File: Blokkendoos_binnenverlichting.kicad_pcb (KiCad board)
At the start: 2 copper layers, 206.8 x 26 mm, 103 parts, among them J1 Conn_01x02, J10 Conn_01x04, J11 Conn_01x04, J12 Conn_01x04, J13 Conn_01x04, J14 Conn_01x04, J15 Conn_01x04, J16 Conn_01x02, J2 Conn_02x11_Counter_Clockwise, J3 Conn_01x04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

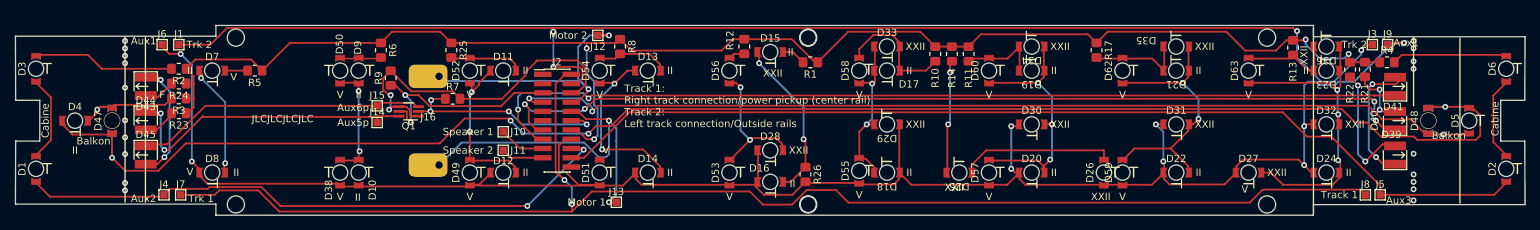
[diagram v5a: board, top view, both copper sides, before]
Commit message: Pulled traces away from edge, making room to cut the corners and/or PCB to shape. Closes #11.
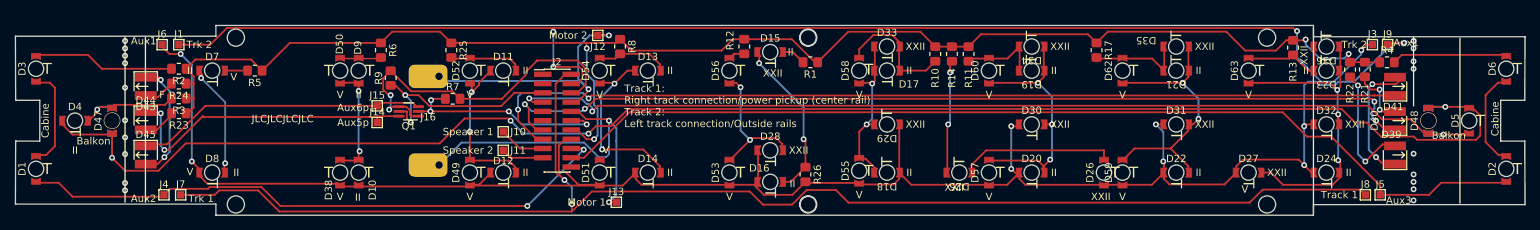
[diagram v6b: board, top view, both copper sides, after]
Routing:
- net Net-(D1-Pad2): track 11.6 -> 14.0 mm
- net Net-(D2-Pad2): track 11.4 -> 13.6 mm
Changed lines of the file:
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@@
   (segment (start 126.882304 132.08) (end 133.113771 125.848533) (width 0.25) (layer "F.Cu") (net 13))
   (segment (start 125.14 132.08) (end 126.882304 132.08) (width 0.25) (layer "F.Cu") (net 13))
-  (segment (start 251.582 137.16) (end 235.966 137.16) (width 0.25) (layer "F.Cu") (net 13))
   (segment (start 225.949786 129.1844) (end 229.2604 129.1844) (width 0.25) (layer "F.Cu") (net 13))
   (segment (start 133.113771 125.848533) (end 222.613919 125.848533) (width 0.25) (layer "F.Cu") (net 13))
+  (segment (start 253.238 135.504) (end 244.317 135.504) (width 0.25) (layer "F.Cu") (net 13))
+  (segment (start 242.661 137.16) (end 235.966 137.16) (width 0.25) (layer "F.Cu") (net 13))
+  (segment (start 244.317 135.504) (end 242.661 137.16) (width 0.25) (layer "F.Cu") (net 13))
   (segment (start 235.966 135.89) (end 235.966 137.16) (width 0.25) (layer "F.Cu") (net 13))
-  (segment (start 253.238 135.504) (end 251.582 137.16) (width 0.25) (layer "F.Cu") (net 13))
-  (segment (start 53.726 137.414) (end 69.088 137.414) (width 0.25) (layer "F.Cu") (net 14))
+  (segment (start 54.904 135.504) (end 56.814 137.414) (width 0.25) (layer "F.Cu") (net 14))
+  (segment (start 56.814 137.414) (end 69.088 137.414) (width 0.25) (layer "F.Cu") (net 14))
+  (segment (start 75.591674 136.0932) (end 82.7024 136.0932) (width 0.25) (layer "F.Cu") (net 14))
+  (segment (start 51.816 135.504) (end 54.904 135.504) (width 0.25) (layer "F.Cu") (net 14))
+  (segment (start 125.14 130.81) (end 126.685402 130.81) (width 0.25) (layer "F.Cu") (net 14))
   (segment (start 69.088 137.414) (end 69.342 137.16) (width 0.25) (layer "F.Cu") (net 14))
-  (segment (start 75.591674 136.0932) (end 82.7024 136.0932) (width 0.25) (layer "F.Cu") (net 14))
-  (segment (start 125.14 130.81) (end 126.685402 130.81) (width 0.25) (layer "F.Cu") (net 14))
   (segment (start 70.166511 136.335489) (end 75.349385 136.335489) (width 0.25) (layer "F.Cu") (net 14))
   (segment (start 85.2932 138.684) (end 119.126 138.684) (width 0.25) (layer "F.Cu") (net 14))
   (segment (start 126.685402 130.81) (end 126.842701 130.967299) (width 0.25) (layer "F.Cu") (net 14))
   (segment (start 82.7024 136.0932) (end 85.2932 138.684) (width 0.25) (layer "F.Cu") (net 14))
-  (segment (start 51.816 135.504) (end 53.726 137.414) (width 0.25) (layer "F.Cu") (net 14))
   (segment (start 69.342 137.16) (end 70.166511 136.335489) (width 0.25) (layer "F.Cu") (net 14))
   (segment (start 75.349385 136.335489) (end 75.591674 136.0932) (width 0.25) (layer "F.Cu") (net 14))
@@
   (segment (start 68.9 126) (end 68.9 130.5) (width 0.25) (layer "B.Cu") (net 54))
   (segment (start 68.9 130.5) (end 69.4 131) (width 0.25) (layer "B.Cu") (net 54))
-  (segment (start 51.816 131.704) (end 53.848 129.672) (width 0.25) (layer "F.Cu") (net 55))
-  (segment (start 53.848 123.82) (end 51.816 121.788) (width 0.25) (layer "F.Cu") (net 55))
-  (segment (start 53.848 129.672) (end 53.848 123.82) (width 0.25) (layer "F.Cu") (net 55))
-  (segment (start 253.238 131.704) (end 251.46 129.926) (width 0.25) (layer "F.Cu") (net 56))
-  (segment (start 251.46 123.566) (end 253.238 121.788) (width 0.25) (layer "F.Cu") (net 56))
-  (segment (start 251.46 129.926) (end 251.46 123.566) (width 0.25) (layer "F.Cu") (net 56))
+  (segment (start 54.4 130.5) (end 54.4 122.5) (width 0.25) (layer "F.Cu") (net 55))
+  (segment (start 54.4 122.5) (end 53.688 121.788) (width 0.25) (layer "F.Cu") (net 55))
+  (segment (start 51.816 131.704) (end 53.196 131.704) (width 0.25) (layer "F.Cu") (net 55))
+  (segment (start 53.196 131.704) (end 54.4 130.5) (width 0.25) (layer "F.Cu") (net 55))
+  (segment (start 53.688 121.788) (end 51.816 121.788) (width 0.25) (layer "F.Cu") (net 55))
+  (segment (start 252.112 121.788) (end 253.238 121.788) (width 0.25) (layer "F.Cu") (net 56))
+  (segment (start 250.4 129.933) (end 250.4 123.5) (width 0.25) (layer "F.Cu") (net 56))
+  (segment (start 250.4 123.5) (end 252.112 121.788) (width 0.25) (layer "F.Cu") (net 56))
+  (segment (start 252.171 131.704) (end 250.4 129.933) (width 0.25) (layer "F.Cu") (net 56))
+  (segment (start 253.238 131.704) (end 252.171 131.704) (width 0.25) (layer "F.Cu") (net 56))
   (segment (start 68.362 128.25) (end 66.04 128.25) (width 0.25) (layer "F.Cu") (net 57))
   (segment (start 70.39 126.222) (end 68.362 128.25) (width 0.25) (layer "F.Cu") (net 57))

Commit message: Added connectors for powerpack and DRC passes, except for silkscreen
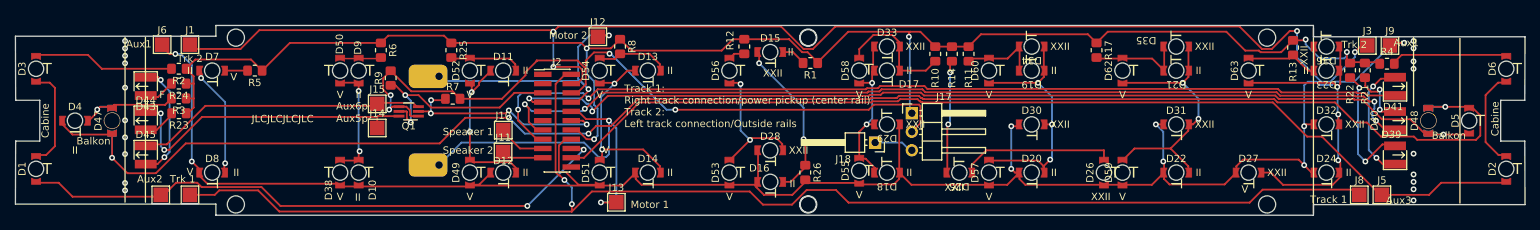
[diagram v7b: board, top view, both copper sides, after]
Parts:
- added J17: Conn_01x03_Female, Connector_PinHeader_2.54mm:PinHeader_1x03_P2.54mm_Horizontal, F.Cu at (171.8, 126.0)
- added J18: Conn_01x01, Connector_PinHeader_2.54mm:PinHeader_1x01_P2.54mm_Horizontal, F.Cu at (166.8, 130.0)
- J1, J10, J11, J12, J13, J14, J15, J3, J4, J5, J6, J7, J8, J9: footprint TestPoint:TestPoint_Pad_1.0x1.0mm -> TestPoint:TestPoint_Pad_2.0x2.0mm
- moved J1 1.53 mm to (72.9, 116.6)
- moved J7 1.27 mm to (72.9, 137.2)
- moved J8 0.83 mm to (233.1, 137.2)
- moved J14 0.75 mm to (98.6, 128.0)
- moved J3 0.71 mm to (234.2, 116.7)
- moved J4 0.44 mm to (68.9, 137.2)
- moved J9 0.34 mm to (237.3, 116.7)
- moved J15 0.27 mm to (98.6, 124.7)
- moved R26 0.27 mm to (157.2, 134.1)
- moved J11 0.24 mm to (115.8, 131.3)
- moved J5 0.23 mm to (236.2, 137.2)
- moved J10 0.22 mm to (115.8, 128.3)
- moved R4 0.20 mm to (236.9, 119.2)
- moved J12 0.18 mm to (128.8, 115.5)
- moved R21 0.12 mm to (233.9, 120.1)
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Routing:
- net GND: track 47.4 -> 102.5 mm, vias 2 -> 4
- net VPP: track 206.4 -> 217.4 mm, vias 4 -> 5
- net /Charge: track 0.00 -> 5.19 mm
- net /Gleis 1: track 189.4 -> 187.1 mm
- net /Motor2: track 48.9 -> 51.1 mm
- net /Gleis 2: track 184.7 -> 186.9 mm
- net Net-(D4-Pad1): track 222.4 -> 224.3 mm
- net /Aux4: track 135.9 -> 137.4 mm
- net Net-(D13-Pad1): track 25.3 -> 26.7 mm
- net /F0r: track 130.7 -> 131.8 mm
- net /F0f: track 128.5 -> 129.6 mm
- net /Aux3: track 136.8 -> 137.5 mm
- net /Aux5: track 29.7 -> 30.3 mm

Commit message: Silkscreen fixes, closes #10
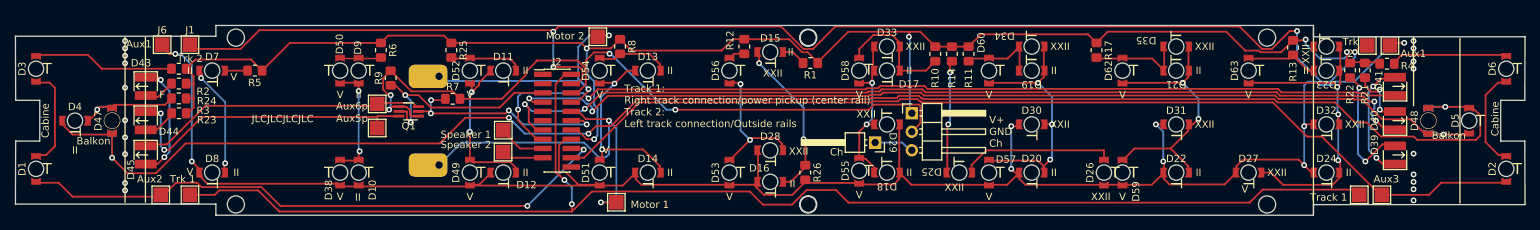
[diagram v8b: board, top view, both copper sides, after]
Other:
- board text added: "Ch"
- board text added: "V+ GND Ch"
